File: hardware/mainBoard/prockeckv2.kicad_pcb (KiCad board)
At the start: 2 copper layers, 100 x 100 mm, 175 parts, among them J1 USB_B_Micro, J10 Screw_Terminal_01x12, J11 Screw_Terminal_01x18, J12 Conn_01x04_Male, J13 Conn_01x04_Male, J14 Conn_01x04_Male, J15 Conn_01x04_Male, J16 Conn_01x05_Male, J17 Conn_01x06_Male, J18 Conn_01x05_Male, J19 Conn_01x06_Male, J2 Screw_Terminal_01x02, J20 Screw_Terminal_01x06, J21 Screw_Terminal_01x02, J22 Screw_Terminal_01x02, J23 Screw_Terminal_01x02, J24 Screw_Terminal_01x02, J25 Conn_01x01_Male, J3 Screw_Terminal_01x19, J4 Screw_Terminal_01x06, J5 MicroSD, J6 Conn_01x06_Male, J7 Conn_01x03_Male, J8 Conn_01x02_Male, J9 Conn_01x03_Male, Q1 FS8205A, Q2 2N7002K, Q3 2N7002K, Q4 S8050, Q5 S8050, Q6 AO3415, Q7 AO3415, Q8 AP2300, Q9 AP2300, SW1 SW_Push, U1 W25Q64JV, U10 RT8279, U11 HX3242, U12 STM32F103VETx, U13 TLC227AIDR, U14 TLC227AIDR, U15 TLC227AIDR, U16 TLC227AIDR, U17 TLC227AIDR, U18 TLC227AIDR, U19 TLC227AIDR, U2 E19-868M30S, U20 TXB0104PW, U3 HY2213, U4 HY2213, U5 HY2120, U6 SGM3204, U7 RT8279, U8 AMS1117-3.3, U9 LM358, Y1 Crystal_GND24

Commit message: PCB finished
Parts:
- added S1: MountingHole_2.2mm_M2_Pad_Via, MountingHole:MountingHole_2.2mm_M2_Pad_Via, F.Cu at (27.7, 102.8)
- added S2: MountingHole_2.2mm_M2_Pad_Via, MountingHole:MountingHole_2.2mm_M2_Pad_Via, F.Cu at (112.6, 163.8)
- C10, C11, C15, C17, C20, C22, C24, C25, C26, C27, C28, C29, C3, C30, C31, C32, C4, C5, C6, C7, C8, D10, D4, D5, D6, D7, D8, D9, J25, J5, L2, Q1, Q4, Q5, Q6, Q7, Q8, Q9, R15, R16, R17, R18, R19, R23, R24, R25, R26, R27, R28, R5, R59, R6, R60, R61, R62, R63, R64, R65, R66, R7, R8, R9, U1, U11, U13, U14, U20, U5, U6, U8, Y1: moved to B.Cu
- J2: footprint TerminalBlock:TerminalBlock_bornier-2_P5.08mm -> Connector_PinSocket_2.54mm:PinSocket_1x02_P2.54mm_Vertical
- J21, J22, J23, J24: footprint TerminalBlock:TerminalBlock_bornier-2_P5.08mm -> Connector_PinHeader_2.54mm:PinHeader_1x02_P2.54mm_Vertical
- J4: footprint TerminalBlock:TerminalBlock_bornier-6_P5.08mm -> Connector_PinSocket_2.54mm:PinSocket_1x06_P2.54mm_Vertical
- J6: footprint Connector_JST:JST_XH_B6B-XH-A_1x06_P2.50mm_Vertical -> Connector_PinHeader_2.54mm:PinHeader_1x06_P2.54mm_Vertical
- moved C23 216.7 mm to (69.9, 136.2)
- moved J9 214.3 mm to (69.3, 128.9)
- moved C26 213.5 mm to (76.1, 124.8), turned to 90 degrees
- moved R22 212.6 mm to (69.9, 137.8)
- moved C29 212.5 mm to (76.1, 128.3), turned to 90 degrees
- moved C31 212.0 mm to (76.9, 120.7)
- moved C25 210.2 mm to (81.2, 129.9)
- moved C30 204.6 mm to (84.6, 129.9), turned to 180 degrees
- moved SW1 199.7 mm to (59.5, 132.6)
- moved C24 199.6 mm to (82.2, 119.6), turned to 180 degrees
- moved R61 199.3 mm to (57.3, 156.8), turned to 180 degrees
- moved C27 197.9 mm to (85.8, 120.5), turned to 270 degrees
- moved F1 196.3 mm to (53.9, 155.9), turned to 90 degrees
- moved C28 194.8 mm to (85.8, 127.4), turned to 90 degrees
- moved R59 184.0 mm to (64.4, 153.8)
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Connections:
- C24 pad 1: Net-(C24-Pad1) -> Net-(U12-Pad12)
- C25 pad 1: Net-(C25-Pad1) -> Net-(U12-Pad13)
- Y1 pad 2: Net-(C24-Pad1) -> GND
- Y1 pad 4: Net-(C25-Pad1) -> GND
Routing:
- net GND: track 184.5 -> 1021.9 mm, vias 4 -> 30
- net +12V: track 70.0 -> 383.4 mm, vias 0 -> 7
- net +3V3: track 0.00 -> 293.7 mm, vias 0 -> 21
- net +5V: track 175.5 -> 385.8 mm, vias 7 -> 16
- net PWR_CTL: track 0.00 -> 111.3 mm, vias 0 -> 3
- net V+: track 0.00 -> 89.8 mm, vias 0 -> 2
- net /IO/IO7: track 0.00 -> 84.2 mm, vias 0 -> 1
- net /IO/IO8: track 0.00 -> 81.7 mm, vias 0 -> 1
- net /IO/IO10: track 0.00 -> 79.4 mm, vias 0 -> 1
- net /MCU/SPI1_2: track 0.00 -> 78.8 mm, vias 0 -> 2
- net /MCU/IO28: track 0.00 -> 77.9 mm, vias 0 -> 4
- net /MCU/IO27: track 0.00 -> 77.6 mm, vias 0 -> 4
- net ~RST: track 0.00 -> 75.8 mm, vias 0 -> 9
- net /MCU/PWM0: track 0.00 -> 73.9 mm, vias 0 -> 4
- net /MCU/SPI1_0: track 0.00 -> 73.5 mm, vias 0 -> 2
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- added copper zone on B.Cu, net GND
- added copper zone on F.Cu, net GND
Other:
- net class Power added: clearance 0.25, trace_width 0.5, via_dia 0.8, via_drill 0.4
- net class Signal added: clearance 0.15, trace_width 0.175, via_dia 0.6, via_drill 0.3
- rule trace_min: 0.2 -> 0.127
- rule via_min_size: 0.2 -> 0.6
- board text added: "FLogger v1"

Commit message: First working software
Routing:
- net +5V: track 385.8 -> 387.6 mm, vias 16 -> 17
- net /MCU/IO23: track 27.7 -> 26.4 mm
- net /MCU/IO24: track 29.2 -> 27.8 mm
- net /MCU/IO21: track 26.8 -> 25.5 mm
- net /MCU/IO20: track 36.0 -> 34.8 mm
- net GND: vias 30 -> 43

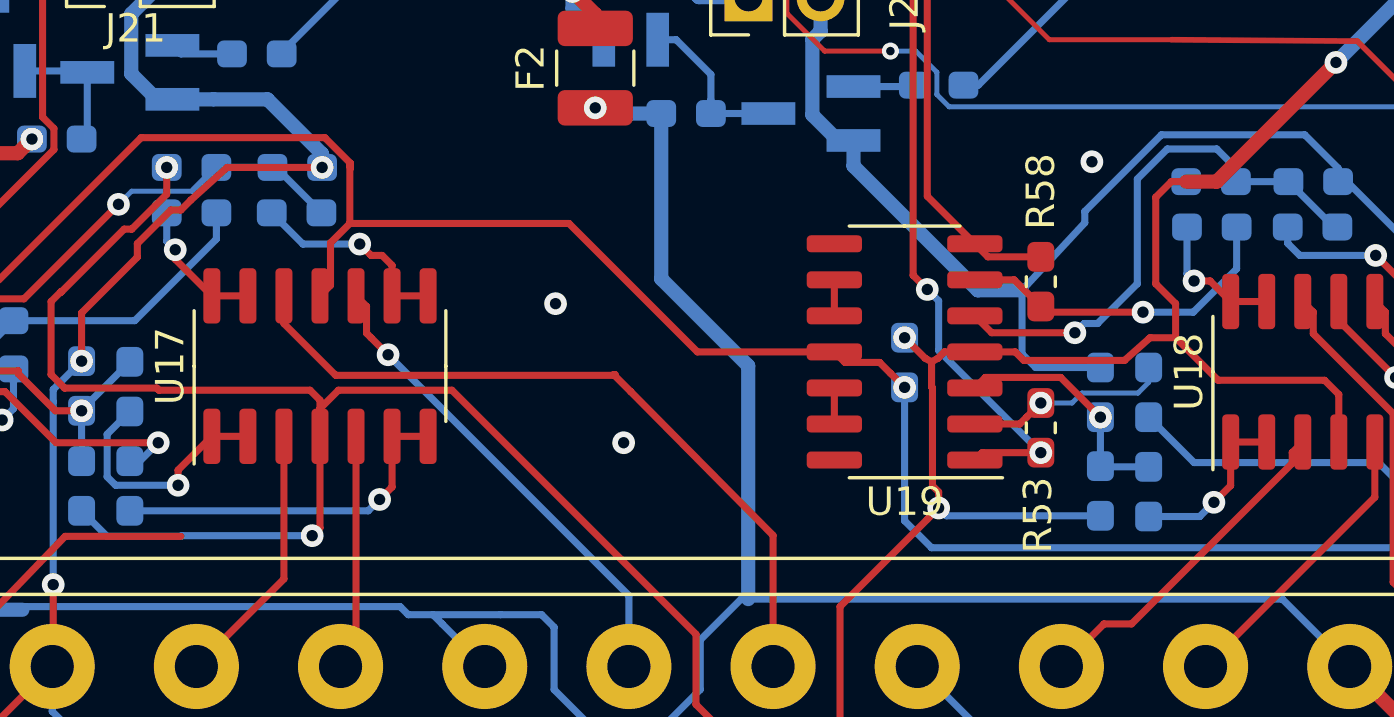
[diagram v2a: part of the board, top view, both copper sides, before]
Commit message: Major changes:  - Added a mutex-like hardware peripheral for SPI  - WIP in Flash driver  - Removed build files  - Added CPP ABI files for virtual functions  - Added an untested SDI12 driver
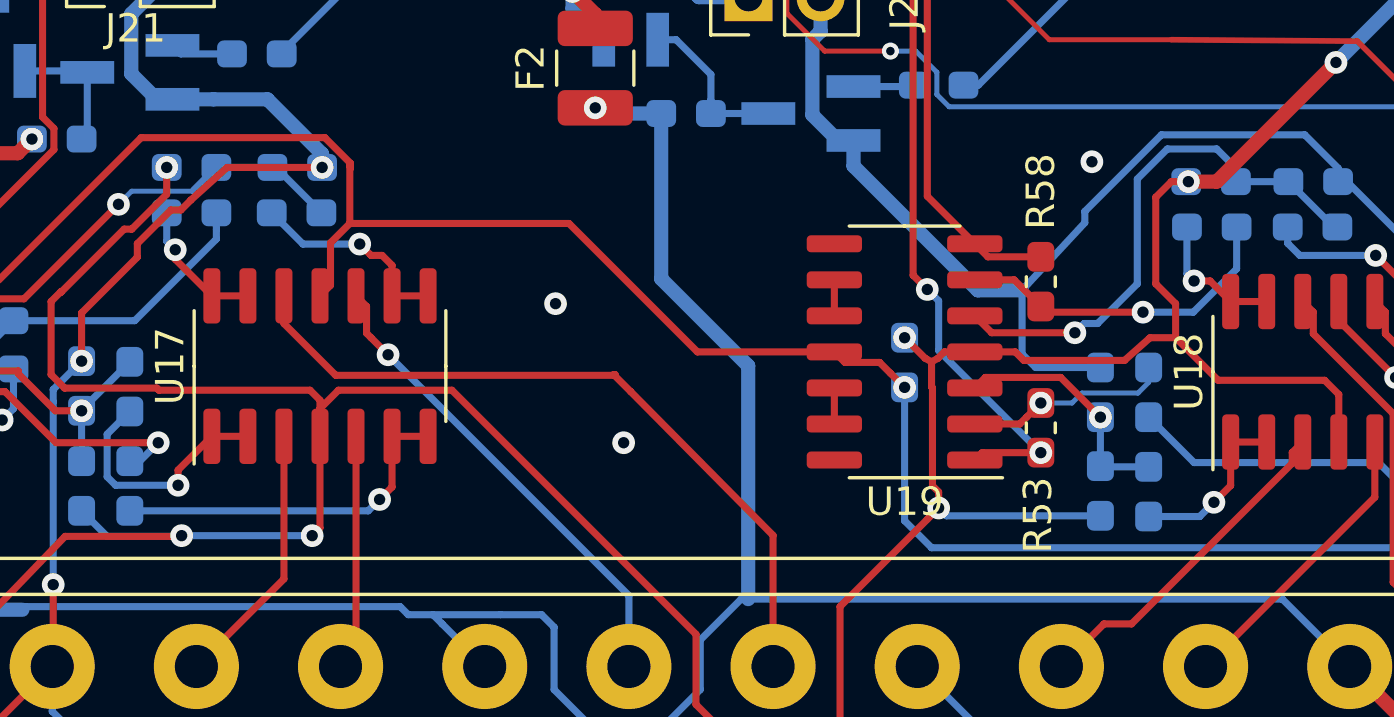
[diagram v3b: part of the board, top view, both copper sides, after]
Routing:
- net +5V: vias 17 -> 19
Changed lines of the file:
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@@
     (thickness 1.6)
     (drawings 5)
-    (tracks 3361)
+    (tracks 3365)
     (zones 0)
     (modules 177)
@@
   (segment (start 29.8 157.95) (end 29.75 158) (width 0.5) (layer B.Cu) (net 8))
   (segment (start 29.8 156.6) (end 29.8 157.95) (width 0.5) (layer B.Cu) (net 8))
-  (segment (start 97.125 158.3) (end 98.2 158.3) (width 0.5) (layer F.Cu) (net 8))
+  (segment (start 97.125 158.3) (end 97.2 158.3) (width 0.5) (layer F.Cu) (net 8))
   (via (at 102.4 154.1) (size 0.8) (drill 0.4) (layers F.Cu B.Cu) (net 8))
   (segment (start 98.2 158.3) (end 102.4 154.1) (width 0.5) (layer F.Cu) (net 8))
@@
   (segment (start 27.75 162.897002) (end 30.575001 160.072001) (width 0.25) (layer F.Cu) (net 8))
   (segment (start 27.75 171.15) (end 27.75 162.897002) (width 0.25) (layer F.Cu) (net 8))
+  (segment (start 61.725 170.775) (end 61.725 170.775) (width 0.25) (layer B.Cu) (net 8))
+  (via (at 61.725 170.775) (size 0.8) (drill 0.4) (layers F.Cu B.Cu) (net 8))
+  (segment (start 97.2 158.3) (end 98.2 158.3) (width 0.5) (layer F.Cu) (net 8))
+  (via (at 97.2 158.3) (size 0.8) (drill 0.4) (layers F.Cu B.Cu) (net 8))
   (segment (start 43.9 120.275) (end 43.9 119.75) (width 0.25) (layer B.Cu) (net 9))
   (segment (start 43.675 120.5) (end 43.9 120.275) (width 0.25) (layer B.Cu) (net 9))
